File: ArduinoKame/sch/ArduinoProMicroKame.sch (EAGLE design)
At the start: 17 parts, among them T1 2N2222, T2 2N2222

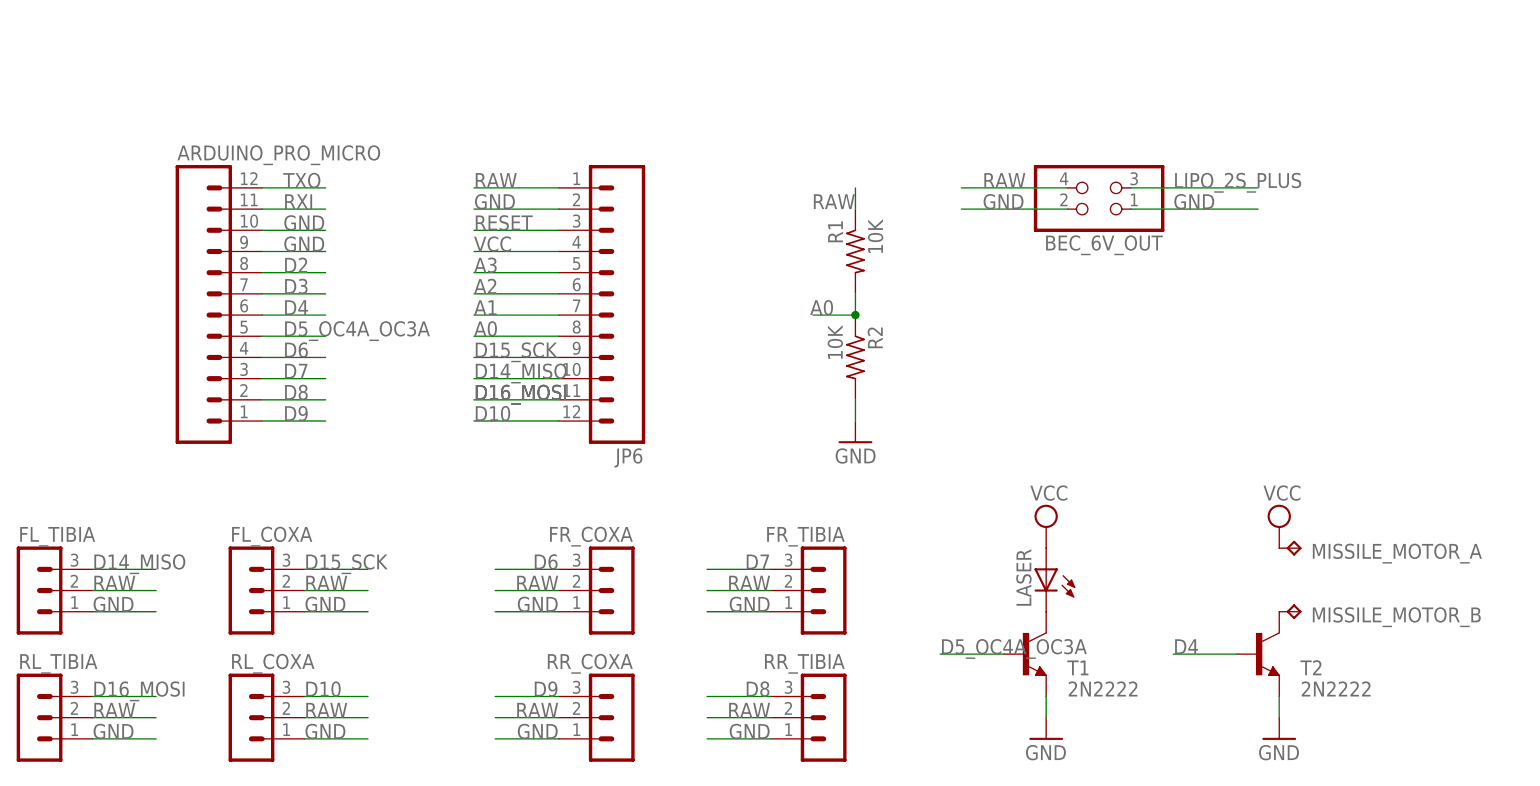
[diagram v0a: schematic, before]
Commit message: buzzer added
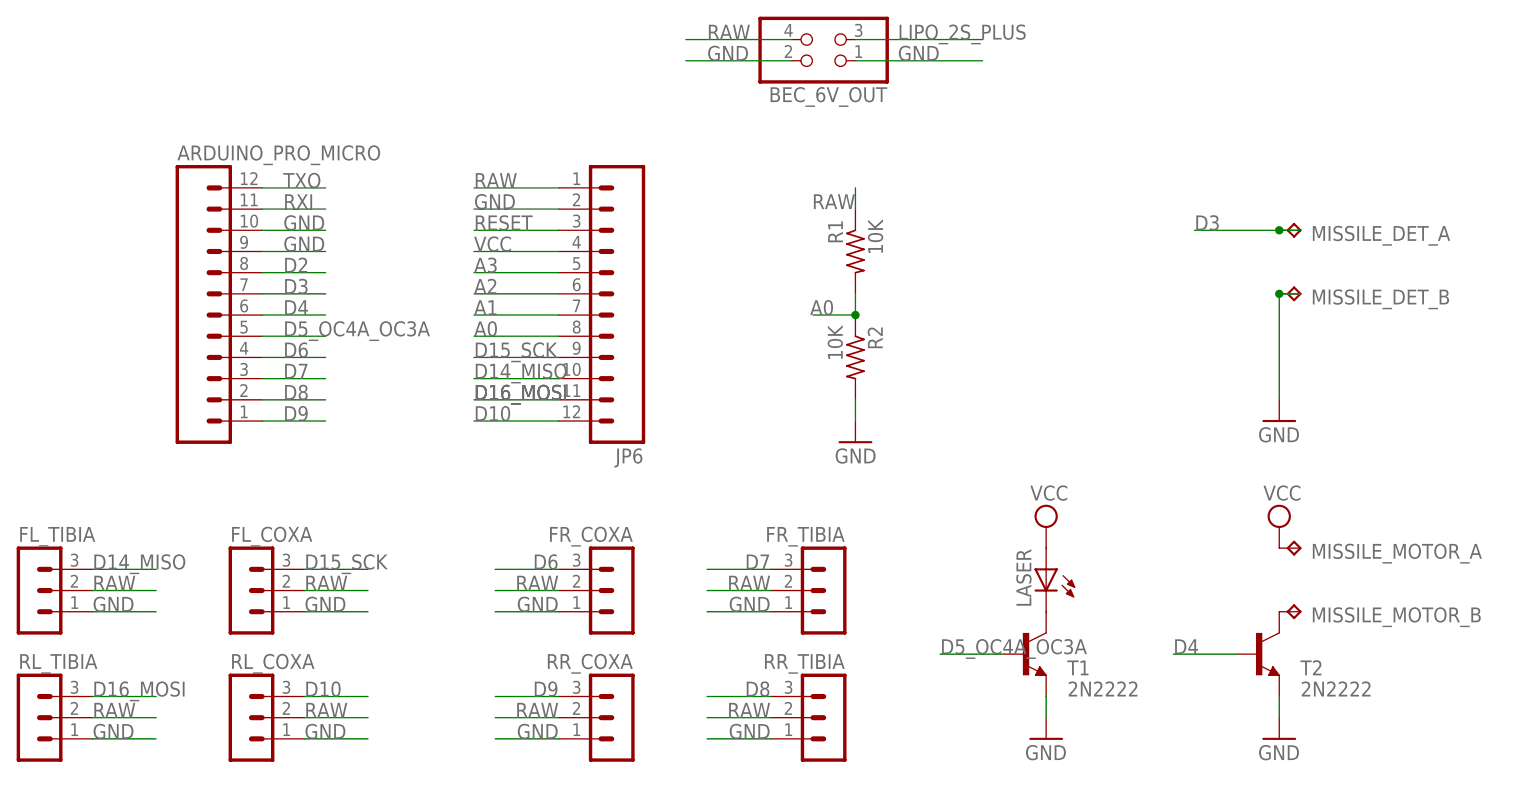
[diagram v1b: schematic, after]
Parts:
- added MISSILE_DET_: TP2P2-38-20, testpad:TP2P2-38-20
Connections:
- net D3: now also MISSILE_DET_A.TP
- net GND: now also MISSILE_DET_B.TP
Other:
- moved on the sheet: BEC_6V_OUT
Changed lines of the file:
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@@
 <part name="GND3" library="supply1" deviceset="GND" device=""/>
 <part name="MISSILE_MOTOR_" library="testpad" deviceset="TP2" device="P2-38-20"/>
+<part name="GND4" library="supply1" deviceset="GND" device=""/>
+<part name="MISSILE_DET_" library="testpad" deviceset="TP2" device="P2-38-20"/>
 </parts>
 <sheets>
@@
 <instance part="RR_TIBIA" gate="G$1" x="104.14" y="7.62" rot="MR0"/>
 <instance part="RR_COXA" gate="G$1" x="78.74" y="7.62" rot="MR0"/>
-<instance part="BEC_6V_OUT" gate="A" x="134.62" y="71.12" rot="R180"/>
+<instance part="BEC_6V_OUT" gate="A" x="101.6" y="88.9" rot="R180"/>
 <instance part="R1" gate="G$1" x="106.68" y="63.5" rot="MR270"/>
 <instance part="R2" gate="G$1" x="106.68" y="50.8" rot="R270"/>
@@
 <attribute name="TP_SIGNAL_NAME" x="158.75" y="19.05" size="1.778" layer="97" rot="R270"/>
 </instance>
+<instance part="GND4" gate="1" x="157.48" y="43.18"/>
+<instance part="MISSILE_DET_" gate="A" x="160.02" y="66.04" smashed="yes" rot="R270">
+<attribute name="NAME" x="161.29" y="64.77" size="1.778" layer="95"/>
+<attribute name="TP_SIGNAL_NAME" x="158.75" y="64.77" size="1.778" layer="97" rot="R270"/>
+</instance>
+<instance part="MISSILE_DET_" gate="B" x="160.02" y="58.42" smashed="yes" rot="R270">
+<attribute name="NAME" x="161.29" y="57.15" size="1.778" layer="95"/>
+<attribute name="TP_SIGNAL_NAME" x="158.75" y="57.15" size="1.778" layer="97" rot="R270"/>
+</instance>
 </instances>
 <busses>
@@
 <segment>
 <pinref part="BEC_6V_OUT" gate="A" pin="2"/>
-<wire x1="132.08" y1="68.58" x2="119.38" y2="68.58" width="0.1524" layer="91"/>
-<label x="121.92" y="68.58" size="1.778" layer="95"/>
+<wire x1="99.06" y1="86.36" x2="86.36" y2="86.36" width="0.1524" layer="91"/>
+<label x="88.9" y="86.36" size="1.778" layer="95"/>
 </segment>
 <segment>
 <pinref part="BEC_6V_OUT" gate="A" pin="1"/>
-<wire x1="139.7" y1="68.58" x2="154.94" y2="68.58" width="0.1524" layer="91"/>
-<label x="144.78" y="68.58" size="1.778" layer="95"/>
+<wire x1="106.68" y1="86.36" x2="121.92" y2="86.36" width="0.1524" layer="91"/>
+<label x="111.76" y="86.36" size="1.778" layer="95"/>
 </segment>
 <segment>
@@
 <pinref part="T2" gate="G$1" pin="E"/>
 <wire x1="157.48" y1="7.62" x2="157.48" y2="10.16" width="0.1524" layer="91"/>
+</segment>
+<segment>
+<pinref part="GND4" gate="1" pin="GND"/>
+<wire x1="160.02" y1="58.42" x2="157.48" y2="58.42" width="0.1524" layer="91"/>
+<wire x1="157.48" y1="58.42" x2="157.48" y2="45.72" width="0.1524" layer="91"/>
+<pinref part="MISSILE_DET_" gate="B" pin="TP"/>
+<junction x="157.48" y="58.42"/>
 </segment>
 </net>
@@
 <segment>
 <pinref part="BEC_6V_OUT" gate="A" pin="4"/>
-<wire x1="132.08" y1="71.12" x2="119.38" y2="71.12" width="0.1524" layer="91"/>
-<label x="121.92" y="71.12" size="1.778" layer="95"/>
+<wire x1="99.06" y1="88.9" x2="86.36" y2="88.9" width="0.1524" layer="91"/>
+<label x="88.9" y="88.9" size="1.778" layer="95"/>
 </segment>
 <segment>
@@
 <pinref part="ARDUINO_PRO_MICRO" gate="G$1" pin="7"/>
 </segment>
+<segment>
+<wire x1="160.02" y1="66.04" x2="157.48" y2="66.04" width="0.1524" layer="91"/>
+<label x="147.32" y="66.04" size="1.778" layer="95"/>
+<pinref part="MISSILE_DET_" gate="A" pin="TP"/>
+<wire x1="157.48" y1="66.04" x2="147.32" y2="66.04" width="0.1524" layer="91"/>
+<junction x="157.48" y="66.04"/>
+</segment>
 </net>
 <net name="D4" class="0">
@@
 <segment>
 <pinref part="BEC_6V_OUT" gate="A" pin="3"/>
-<wire x1="139.7" y1="71.12" x2="154.94" y2="71.12" width="0.1524" layer="91"/>
-<label x="144.78" y="71.12" size="1.778" layer="95"/>
-</segment>
-</net>
+<wire x1="106.68" y1="88.9" x2="121.92" y2="88.9" width="0.1524" layer="91"/>
+<label x="111.76" y="88.9" size="1.778" layer="95"/>
+</segment>
+</net>
